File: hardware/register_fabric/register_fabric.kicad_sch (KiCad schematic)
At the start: 417 parts, among them J2 Conn_02x40_Odd_Even, J3 Conn_02x16_Odd_Even, J4 Conn_02x16_Odd_Even, J5 Conn_02x16_Odd_Even, J6 Conn_02x16_Odd_Even, J7 Conn_02x16_Odd_Even, J8 Conn_02x16_Odd_Even, J9 Conn_02x16_Odd_Even, Q109 IRLML6244, Q110 IRLML6402, Q111 IRLML6244, Q112 IRLML6402, Q113 IRLML6244, Q114 IRLML6402, Q115 IRLML6244, Q116 IRLML6402, Q117 IRLML6244, Q118 IRLML6402, Q119 IRLML6244, Q120 IRLML6402, Q121 IRLML6244, Q122 IRLML6402, Q123 IRLML6244, Q124 IRLML6402, Q125 IRLML6244, Q126 IRLML6402, Q127 IRLML6244, Q128 IRLML6402, Q129 IRLML6244, Q130 IRLML6402, Q131 IRLML6244, Q132 IRLML6402, Q133 IRLML6244, Q134 IRLML6402, Q135 IRLML6244, Q136 IRLML6402, Q137 IRLML6244, Q138 IRLML6402, Q139 IRLML6244, Q140 IRLML6402, Q141 IRLML6244, Q142 IRLML6402, Q143 IRLML6244, Q144 IRLML6402, Q145 IRLML6244, Q146 IRLML6402, Q147 IRLML6244, Q148 IRLML6402, Q149 IRLML6244, Q150 IRLML6402, Q151 IRLML6244, Q152 IRLML6402, Q153 IRLML6244, Q154 IRLML6402, Q155 IRLML6244, Q156 IRLML6402, Q157 IRLML6244, Q158 IRLML6402, Q159 IRLML6244, Q160 IRLML6402, Q161 IRLML6244, Q162 IRLML6402, Q163 IRLML6244, Q164 IRLML6402, Q165 IRLML6244, Q166 IRLML6402, Q167 IRLML6244, Q168 IRLML6402, Q169 IRLML6244, Q170 IRLML6402, Q171 IRLML6244, Q172 IRLML6402, Q173 IRLML6244, Q174 IRLML6402, Q175 IRLML6244, Q176 IRLML6402, Q177 IRLML6244, Q178 IRLML6402, Q179 IRLML6244, Q180 IRLML6402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

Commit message: fixed ALU order of Op bits, finished register fabric schematic
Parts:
- removed R244, R245, R246, R247, R248, R249, R250, R251, R252, R253, R254, R255, R256, R257, R258, R259: 1000, Resistor_SMD:R_0402_1005Metric, symbol Device:R
- added R1, R10, R11, R12, R13, R14, R15, R16, R2, R3, R4, R5, R6, R7, R8, R9: 10K, Resistor_SMD:R_0402_1005Metric, symbol Device:R
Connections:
- net +5V: now also R1.1, R10.1, R11.1, R12.1, R13.1, R14.1, R15.1, R16.1, R2.1, R3.1, R4.1, R5.1, R6.1, R7.1, R8.1, R9.1
- net RWEN: now also J2.76 (Pin_76); no longer J2.74 (Pin_74)
- net RSI10: now reaches D194.2 (A), Q216.3 (D), U18.1 (A0)
- net IRWEN: now reaches U19.1, U21.1, U22.1, U23.1, U24.1, U25.1, U26.1
- net IRWEN: now also D198.2 (A), Q224.3 (D)
- net FII2: now reaches D170.2 (A), Q168.3 (D), U89.10 (I1c)
- net at U17.19 (CE), U18.7 (~{Y7}): now also R16.2
- net DII2: now reaches D146.2 (A), J3.15 (Pin_15), J4.15 (Pin_15), J5.15 (Pin_15), J6.15 (Pin_15), J8.15 (Pin_15), J9.15 (Pin_15), Q120.3 (D), U89.11 (I0c)
- net DII1: now reaches D147.2 (A), J3.14 (Pin_14), J4.14 (Pin_14), J5.14 (Pin_14), J6.14 (Pin_14), J8.14 (Pin_14), J9.14 (Pin_14), Q122.3 (D), U89.5 (I0b)
- net WSI0: now reaches D197.2 (A), Q222.3 (D), U20.1 (A0)
- net IFWEN: now reaches D199.2 (A), Q226.3 (D), U24.10, U24.9, U89.1 (S), U90.1 (S)
- net FII3: now reaches D169.2 (A), Q166.3 (D), U89.13 (I1d)
- net DII3: now reaches D145.2 (A), J3.16 (Pin_16), J4.16 (Pin_16), J5.16 (Pin_16), J6.16 (Pin_16), J8.16 (Pin_16), J9.16 (Pin_16), Q118.3 (D), U89.14 (I0d)
- net DII0: now reaches D148.2 (A), J3.13 (Pin_13), J4.13 (Pin_13), J5.13 (Pin_13), J6.13 (Pin_13), J8.13 (Pin_13), J9.13 (Pin_13), Q124.3 (D), U89.2 (I0a)
- net FII0: now reaches D172.2 (A), Q172.3 (D), U89.3 (I1a)
- net FII1: now reaches D171.2 (A), Q170.3 (D), U89.6 (I1b)
- net RAI8: now reaches Q187.1 (G)
- net RAI8: now also J9.3 (Pin_3), U16.2 (A0), U17.2 (A0)
- net RI07: now reaches Q125.1 (G), U1.11 (B7), U10.11 (B7), U12.11 (B7), U14.11 (B7), U16.11 (B7), U4.11 (B7), U6.11 (B7), U8.11 (B7)
- net RI06: now reaches Q127.1 (G), U1.12 (B6), U10.12 (B6), U12.12 (B6), U14.12 (B6), U16.12 (B6), U4.12 (B6), U6.12 (B6), U8.12 (B6)
- net RI05: now reaches Q129.1 (G), U1.13 (B5), U10.13 (B5), U12.13 (B5), U14.13 (B5), U16.13 (B5), U4.13 (B5), U6.13 (B5), U8.13 (B5)
- net RI04: now reaches Q131.1 (G), U1.14 (B4), U10.14 (B4), U12.14 (B4), U14.14 (B4), U16.14 (B4), U4.14 (B4), U6.14 (B4), U8.14 (B4)
- net RI03: now reaches Q133.1 (G), U1.15 (B3), U10.15 (B3), U12.15 (B3), U14.15 (B3), U16.15 (B3), U4.15 (B3), U6.15 (B3), U8.15 (B3)
- net RI02: now reaches Q135.1 (G), U1.16 (B2), U10.16 (B2), U12.16 (B2), U14.16 (B2), U16.16 (B2), U4.16 (B2), U6.16 (B2), U8.16 (B2)
- net RI01: now reaches Q137.1 (G), U1.17 (B1), U10.17 (B1), U12.17 (B1), U14.17 (B1), U16.17 (B1), U4.17 (B1), U6.17 (B1), U8.17 (B1)
- net RI00: now reaches Q139.1 (G), U1.18 (B0), U10.18 (B0), U12.18 (B0), U14.18 (B0), U16.18 (B0), U4.18 (B0), U6.18 (B0), U8.18 (B0)
- net at U14.19 (CE), U2.9 (~{Y6}): now also R13.2
- net RAI0: now reaches J8.3 (Pin_3), U14.2 (A0), U15.2 (A0)
- net RAI0: now also Q203.1 (G)
- net RAI1: now reaches J8.4 (Pin_4), U14.3 (A1), U15.3 (A1)
- net RAI1: now also Q201.1 (G)
- net RAI2: now reaches J8.5 (Pin_5), U14.4 (A2), U15.4 (A2)
- net RAI2: now also Q199.1 (G)
- net RAI3: now reaches J8.6 (Pin_6), U14.5 (A3), U15.5 (A3)
- net RAI3: now also Q197.1 (G)
- net RAI4: now reaches J8.7 (Pin_7), U14.6 (A4), U15.6 (A4)
- net RAI4: now also Q195.1 (G)
- net RAI5: now reaches J8.8 (Pin_8), U14.7 (A5), U15.7 (A5)
- net RAI5: now also Q193.1 (G)
- net RAI6: now reaches J8.9 (Pin_9), U14.8 (A6), U15.8 (A6)
- net RAI6: now also Q191.1 (G)
- net RAI7: now reaches J8.10 (Pin_10), U14.9 (A7), U15.9 (A7)
- net RAI7: now also Q189.1 (G)
- net FII5: now reaches D167.2 (A), Q162.3 (D), U90.6 (I1b)
- net at U12.19 (CE), U2.10 (~{Y5}): now also R11.2
- net COUT: now reaches J7.5 (Pin_5), U12.4 (A2), U13.4 (A2)
- net COUT: now also J2.74 (Pin_74)
- net WSI1: now reaches D196.2 (A), Q220.3 (D), U20.2 (A1)
- net RSI02: now reaches D189.2 (A), Q206.3 (D), U2.3 (A2)
- net RI12: now reaches Q151.1 (G), U11.16 (B2), U13.16 (B2), U15.16 (B2), U17.16 (B2), U3.16 (B2), U5.16 (B2), U7.16 (B2), U9.16 (B2)
- net RSI11: now reaches D193.2 (A), Q214.3 (D), U18.2 (A1)
- net RI17: now reaches Q141.1 (G), U11.11 (B7), U13.11 (B7), U15.11 (B7), U17.11 (B7), U3.11 (B7), U5.11 (B7), U7.11 (B7), U9.11 (B7)
- net RI16: now reaches Q143.1 (G), U11.12 (B6), U13.12 (B6), U15.12 (B6), U17.12 (B6), U3.12 (B6), U5.12 (B6), U7.12 (B6), U9.12 (B6)
- net RI15: now reaches Q145.1 (G), U11.13 (B5), U13.13 (B5), U15.13 (B5), U17.13 (B5), U3.13 (B5), U5.13 (B5), U7.13 (B5), U9.13 (B5)
- net RI14: now reaches Q147.1 (G), U11.14 (B4), U13.14 (B4), U15.14 (B4), U17.14 (B4), U3.14 (B4), U5.14 (B4), U7.14 (B4), U9.14 (B4)
- net RI13: now reaches Q149.1 (G), U11.15 (B3), U13.15 (B3), U15.15 (B3), U17.15 (B3), U3.15 (B3), U5.15 (B3), U7.15 (B3), U9.15 (B3)
- net RI11: now reaches Q153.1 (G), U11.17 (B1), U13.17 (B1), U15.17 (B1), U17.17 (B1), U3.17 (B1), U5.17 (B1), U7.17 (B1), U9.17 (B1)
- net RI10: now reaches Q155.1 (G), U11.18 (B0), U13.18 (B0), U15.18 (B0), U17.18 (B0), U3.18 (B0), U5.18 (B0), U7.18 (B0), U9.18 (B0)
- net at U15.19 (CE), U18.9 (~{Y6}): now also R14.2
- net FII6: now reaches D166.2 (A), Q160.3 (D), U90.10 (I1c)
- net FII7: now reaches D165.2 (A), Q158.3 (D), U90.13 (I1d)
- net at J2.2 (Pin_2), J2.20 (Pin_20), J2.38 (Pin_38)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: no longer J2.76 (Pin_76)
- net RSI00: now reaches D191.2 (A), Q210.3 (D), U2.1 (A0)
- net DII4: now reaches D144.2 (A), J3.17 (Pin_17), J4.17 (Pin_17), J5.17 (Pin_17), J6.17 (Pin_17), J8.17 (Pin_17), J9.17 (Pin_17), Q116.3 (D), U90.2 (I0a)
- net DII5: now reaches D143.2 (A), J3.18 (Pin_18), J4.18 (Pin_18), J5.18 (Pin_18), J6.18 (Pin_18), J8.18 (Pin_18), J9.18 (Pin_18), Q114.3 (D), U90.5 (I0b)
- net DII6: now reaches D142.2 (A), J3.19 (Pin_19), J4.19 (Pin_19), J5.19 (Pin_19), J6.19 (Pin_19), J8.19 (Pin_19), J9.19 (Pin_19), Q112.3 (D), U90.11 (I0c)
- net DII7: now reaches D141.2 (A), J3.20 (Pin_20), J4.20 (Pin_20), J5.20 (Pin_20), J6.20 (Pin_20), J8.20 (Pin_20), J9.20 (Pin_20), Q110.3 (D), U90.14 (I0d)
- net ICLK: now reaches D200.2 (A), J3.25 (Pin_25), J4.25 (Pin_25), J5.25 (Pin_25), J6.25 (Pin_25), J7.25 (Pin_25), J8.25 (Pin_25), J9.25 (Pin_25), Q228.3 (D)
- net I!CLR: now reaches D201.2 (A), J3.29 (Pin_29), J4.29 (Pin_29), J5.29 (Pin_29), J6.29 (Pin_29), J7.29 (Pin_29), J8.29 (Pin_29), J9.29 (Pin_29), Q230.3 (D)
- net at U16.19 (CE), U2.7 (~{Y7}): now also R15.2
- net at U2.14 (~{Y1}), U4.19 (CE): now also R3.2
- net RAI11: now reaches Q181.1 (G)
- net RAI11: now also J9.6 (Pin_6), U16.5 (A3), U17.5 (A3)
- net RSI12: now reaches D192.2 (A), Q212.3 (D), U18.3 (A2)
- net RAI9: now reaches Q185.1 (G)
- net RAI9: now also J9.4 (Pin_4), U16.3 (A1), U17.3 (A1)
- net at U10.19 (CE), U2.11 (~{Y4}): now also R9.2
- net WSI2: now reaches D195.2 (A), Q218.3 (D), U20.3 (A2)
- net at U18.14 (~{Y1}), U5.19 (CE): now also R4.2
- net RAI15: now reaches J9.10 (Pin_10), U16.9 (A7), U17.9 (A7)
- net RAI15: now also Q173.1 (G)
- net RAI10: now reaches J9.5 (Pin_5), U16.4 (A2), U17.4 (A2)
- net RAI10: now also Q183.1 (G)
- net RAI12: now reaches J9.7 (Pin_7), U16.6 (A4), U17.6 (A4)
- net RAI12: now also Q179.1 (G)
- net RAI13: now reaches J9.8 (Pin_8), U16.7 (A5), U17.7 (A5)
- net RAI13: now also Q177.1 (G)
- net RAI14: now reaches J9.9 (Pin_9), U16.8 (A6), U17.8 (A6)
- net RAI14: now also Q175.1 (G)
- net at U11.19 (CE), U18.11 (~{Y4}): now also R10.2
- net at U18.13 (~{Y2}), U7.19 (CE): now also R6.2
- net at U2.13 (~{Y2}), U6.19 (CE): now also R5.2
- net at U13.19 (CE), U18.10 (~{Y5}): now also R12.2
- net RSI01: now reaches D190.2 (A), Q208.3 (D), U2.2 (A1)
- net at U18.12 (~{Y3}), U9.19 (CE): now also R8.2
- net at U2.12 (~{Y3}), U8.19 (CE): now also R7.2
- net at U18.15 (~{Y0}), U3.19 (CE): now also R2.2
- net at U1.19 (CE), U2.15 (~{Y0}): now also R1.2
- net FII4: now reaches D168.2 (A), Q164.3 (D), U90.3 (I1a)
- no-connect marks 13 -> 15
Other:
- moved on the sheet: C2, C25, C3

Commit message: started work on register fabric PCB layout, grouped LEDs
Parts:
- U1, U10, U11, U12, U13, U14, U15, U16, U17, U3, U4, U5, U6, U7, U8, U9: footprint Package_SO:SO-20_12.8x7.5mm_P1.27mm -> Package_SO:TSSOP-20_4.4x6.5mm_P0.65mm
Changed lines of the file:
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@@
 			)
 		)
-		(property "Footprint" "Package_SO:SO-20_12.8x7.5mm_P1.27mm"
+		(property "Footprint" "Package_SO:TSSOP-20_4.4x6.5mm_P0.65mm"
 			(at 1671.32 1037.59 0)
 			(effects
@@
 			)
 		)
-		(property "Footprint" "Package_SO:SO-20_12.8x7.5mm_P1.27mm"
+		(property "Footprint" "Package_SO:TSSOP-20_4.4x6.5mm_P0.65mm"
 			(at 1671.32 920.75 0)
 			(effects
@@
 			)
 		)
-		(property "Footprint" "Package_SO:SO-20_12.8x7.5mm_P1.27mm"
+		(property "Footprint" "Package_SO:TSSOP-20_4.4x6.5mm_P0.65mm"
 			(at 1671.32 1096.01 0)
 			(effects
@@
 			)
 		)
-		(property "Footprint" "Package_SO:SO-20_12.8x7.5mm_P1.27mm"
+		(property "Footprint" "Package_SO:TSSOP-20_4.4x6.5mm_P0.65mm"
 			(at 1671.32 862.33 0)
 			(effects
@@
 			)
 		)
-		(property "Footprint" "Package_SO:SO-20_12.8x7.5mm_P1.27mm"
+		(property "Footprint" "Package_SO:TSSOP-20_4.4x6.5mm_P0.65mm"
 			(at 1671.32 570.23 0)
 			(effects
@@
 			)
 		)
-		(property "Footprint" "Package_SO:SO-20_12.8x7.5mm_P1.27mm"
+		(property "Footprint" "Package_SO:TSSOP-20_4.4x6.5mm_P0.65mm"
 			(at 1671.32 979.17 0)
 			(effects
@@
 			)
 		)
-		(property "Footprint" "Package_SO:SO-20_12.8x7.5mm_P1.27mm"
+		(property "Footprint" "Package_SO:TSSOP-20_4.4x6.5mm_P0.65mm"
 			(at 1671.32 803.91 0)
 			(effects
@@
 			)
 		)
-		(property "Footprint" "Package_SO:SO-20_12.8x7.5mm_P1.27mm"
+		(property "Footprint" "Package_SO:TSSOP-20_4.4x6.5mm_P0.65mm"
 			(at 1671.32 745.49 0)
 			(effects
@@
 			)
 		)
-		(property "Footprint" "Package_SO:SO-20_12.8x7.5mm_P1.27mm"
+		(property "Footprint" "Package_SO:TSSOP-20_4.4x6.5mm_P0.65mm"
 			(at 1671.32 394.97 0)
 			(effects
@@
 			)
 		)
-		(property "Footprint" "Package_SO:SO-20_12.8x7.5mm_P1.27mm"
+		(property "Footprint" "Package_SO:TSSOP-20_4.4x6.5mm_P0.65mm"
 			(at 1671.32 1154.43 0)
 			(effects
@@
 			)
 		)
-		(property "Footprint" "Package_SO:SO-20_12.8x7.5mm_P1.27mm"
+		(property "Footprint" "Package_SO:TSSOP-20_4.4x6.5mm_P0.65mm"
 			(at 1671.32 1212.85 0)
 			(effects
@@
 			)
 		)
-		(property "Footprint" "Package_SO:SO-20_12.8x7.5mm_P1.27mm"
+		(property "Footprint" "Package_SO:TSSOP-20_4.4x6.5mm_P0.65mm"
 			(at 1671.32 687.07 0)
 			(effects
@@
 		(on_board yes)
 		(dnp no)
-		(fields_autoplaced yes)
 		(property "Reference" "U4"
 			(at 1673.4633 433.07 0)
@@
 			)
 		)
-		(property "Footprint" "Package_SO:SO-20_12.8x7.5mm_P1.27mm"
+		(property "Footprint" "Package_SO:TSSOP-20_4.4x6.5mm_P0.65mm"
 			(at 1671.32 453.39 0)
 			(effects
@@
 			)
 		)
-		(property "Footprint" "Package_SO:SO-20_12.8x7.5mm_P1.27mm"
+		(property "Footprint" "Package_SO:TSSOP-20_4.4x6.5mm_P0.65mm"
 			(at 1671.32 628.65 0)
 			(effects
@@
 			)
 		)
-		(property "Footprint" "Package_SO:SO-20_12.8x7.5mm_P1.27mm"
+		(property "Footprint" "Package_SO:TSSOP-20_4.4x6.5mm_P0.65mm"
 			(at 1671.32 511.81 0)
 			(effects
@@
 			)
 		)
-		(property "Footprint" "Package_SO:SO-20_12.8x7.5mm_P1.27mm"
+		(property "Footprint" "Package_SO:TSSOP-20_4.4x6.5mm_P0.65mm"
 			(at 1671.32 336.55 0)
 			(effects

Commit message: finished Rev A of register fabric pcb
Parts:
- added C33, C34, C35, C36: 330nF, Capacitor_SMD:C_0402_1005Metric, symbol Device:C
- added D202: LED, LED_SMD:LED_0402_1005Metric, symbol Device:LED
- added R244: 1000, Resistor_SMD:R_0402_1005Metric, symbol Device:R
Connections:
- net +5V: now also C33.1, C34.1, C35.1, C36.1, D202.2 (A)
- net GND: now also J2.1 (Pin_1), J2.19 (Pin_19), J2.2 (Pin_2), J2.20 (Pin_20), J2.37 (Pin_37), J2.38 (Pin_38), J2.55 (Pin_55), J2.56 (Pin_56), J2.63 (Pin_63), J2.64 (Pin_64), J2.69 (Pin_69), J2.72 (Pin_72), J2.79 (Pin_79), J2.80 (Pin_80), C33.2, C34.2, C35.2, C36.2, R244.1
- new net: D202.1 (K), R244.2

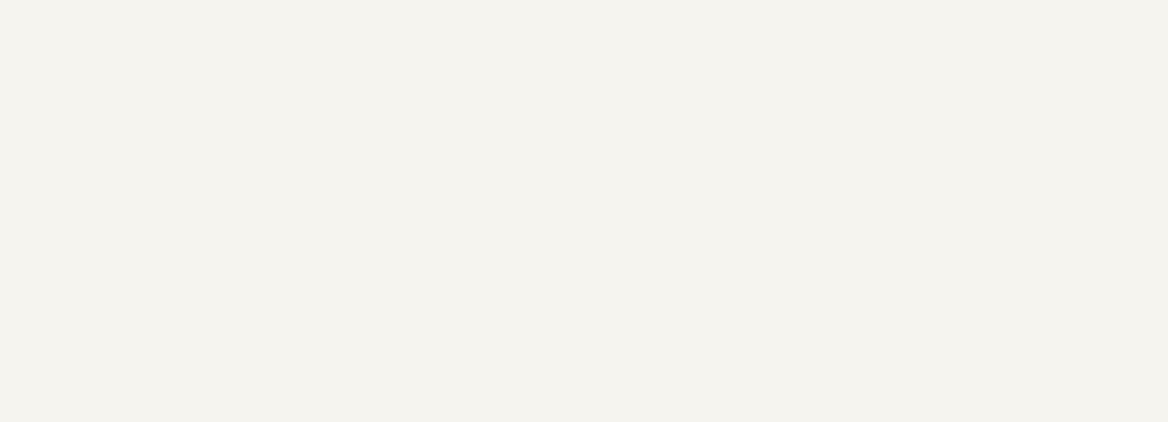
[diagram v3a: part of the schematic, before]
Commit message: added fiducials and markers to ALU, started on register fabric
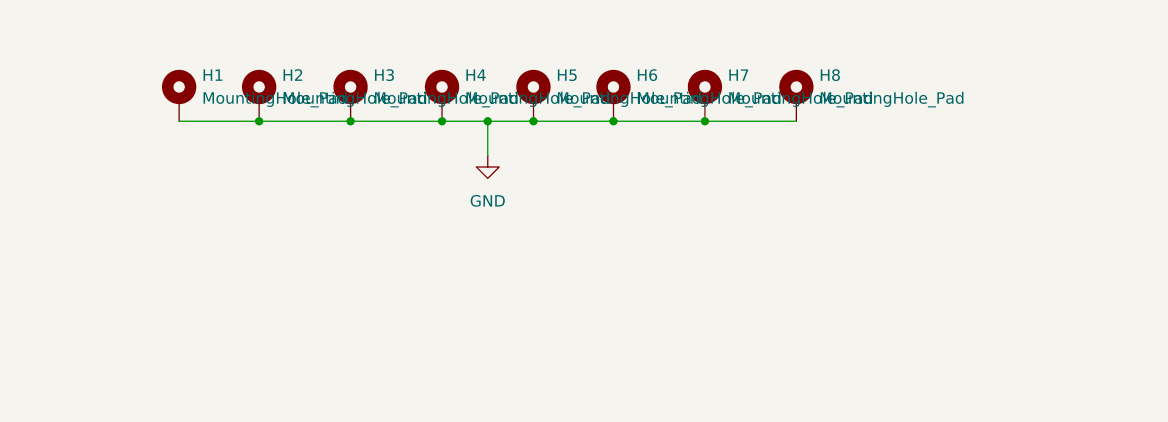
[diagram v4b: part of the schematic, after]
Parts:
- added H1, H2, H3, H4, H5, H6, H7, H8: MountingHole_Pad, MountingHole:MountingHole_3.2mm_M3_ISO7380_Pad_TopBottom, symbol Mechanical:MountingHole_Pad
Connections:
- net GND: now also H1.1, H2.1, H3.1, H4.1, H5.1, H6.1, H7.1, H8.1

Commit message: small fixes on register fabric
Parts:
- R1, R10, R11, R12, R13, R14, R15, R16, R2, R21, R22, R23, R24, R25, R26, R27, R28, R29, R3, R30, R31, R32, R33, R34, R35, R36, R37, R38, R39, R4, R40, R41, R45, R46, R47, R48, R49, R5, R50, R51, R52, R6, R7, R8, R9: value 10K -> 100K
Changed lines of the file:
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@@
 			)
 		)
-		(property "Value" "10K"
+		(property "Value" "100K"
 			(at 1630.68 1046.48 90)
 			(effects
@@
 			)
 		)
-		(property "Value" "10K"
+		(property "Value" "100K"
 			(at 424.18 807.7199 0)
 			(effects
@@
 			)
 		)
-		(property "Value" "10K"
+		(property "Value" "100K"
 			(at 553.72 807.7199 0)
 			(effects
@@
 			)
 		)
-		(property "Value" "10K"
+		(property "Value" "100K"
 			(at 643.89 384.8099 0)
 			(effects
@@
 			)
 		)
-		(property "Value" "10K"
+		(property "Value" "100K"
 			(at 904.24 384.8099 0)
 			(effects
@@
 			)
 		)
-		(property "Value" "10K"
+		(property "Value" "100K"
 			(at 1621.79 520.7 90)
 			(effects
@@
 			)
 		)
-		(property "Value" "10K"
+		(property "Value" "100K"
 			(at 294.64 386.0799 0)
 			(effects
@@
 			)
 		)
-		(property "Value" "10K"
+		(property "Value" "100K"
 			(at 337.82 386.0799 0)
 			(effects
@@
 			)
 		)
-		(property "Value" "10K"
+		(property "Value" "100K"
 			(at 596.9 933.4499 0)
 			(effects
@@
 			)
 		)
-		(property "Value" "10K"
+		(property "Value" "100K"
 			(at 1630.68 1104.9 90)
 			(effects
@@
 			)
 		)
-		(property "Value" "10K"
+		(property "Value" "100K"
 			(at 1621.79 988.06 90)
 			(effects
@@
 			)
 		)
-		(property "Value" "10K"
+		(property "Value" "100K"
 			(at 1621.79 754.38 90)
 			(effects
@@
 			)
 		)
-		(property "Value" "10K"
+		(property "Value" "100K"
 			(at 817.88 384.8099 0)
 			(effects
@@
 			)
 		)
-		(property "Value" "10K"
+		(property "Value" "100K"
 			(at 1621.79 579.12 90)
 			(effects
@@
 			)
 		)
-		(property "Value" "10K"
+		(property "Value" "100K"
 			(at 510.54 807.7199 0)
 			(effects
@@
 			)
 		)
-		(property "Value" "10K"
+		(property "Value" "100K"
 			(at 553.72 933.4499 0)
 			(effects
@@
 			)
 		)
-		(property "Value" "10K"
+		(property "Value" "100K"
 			(at 1630.68 1163.32 90)
 			(effects
@@
 			)
 		)
-		(property "Value" "10K"
+		(property "Value" "100K"
 			(at 337.82 807.7199 0)
 			(effects
@@
 			)
 		)
-		(property "Value" "10K"
+		(property "Value" "100K"
 			(at 1621.79 403.86 90)
 			(effects
@@
 			)
 		)
-		(property "Value" "10K"
+		(property "Value" "100K"
 			(at 1621.79 871.22 90)
 			(effects
@@
 			)
 		)
-		(property "Value" "10K"
+		(property "Value" "100K"
 			(at 424.18 933.4499 0)
 			(effects
@@
 			)
 		)
-		(property "Value" "10K"
+		(property "Value" "100K"
 			(at 687.07 384.8099 0)
 			(effects
@@
 			)
 		)
-		(property "Value" "10K"
+		(property "Value" "100K"
 			(at 467.36 386.0799 0)
 			(effects
@@
 			)
 		)
-		(property "Value" "10K"
+		(property "Value" "100K"
 			(at 1621.79 637.54 90)
 			(effects
@@
 			)
 		)
-		(property "Value" "10K"
+		(property "Value" "100K"
 			(at 730.25 384.8099 0)
 			(effects
@@
 			)
 		)
-		(property "Value" "10K"
+		(property "Value" "100K"
 			(at 947.42 384.8099 0)
 			(effects
@@
 			)
 		)
-		(property "Value" "10K"
+		(property "Value" "100K"
 			(at 596.9 807.7199 0)
 			(effects
@@
 			)
 		)
-		(property "Value" "10K"
+		(property "Value" "100K"
 			(at 294.64 933.4499 0)
 			(effects
@@
 			)
 		)
-		(property "Value" "10K"
+		(property "Value" "100K"
 			(at 337.82 933.4499 0)
 			(effects
@@
 			)
 		)
-		(property "Value" "10K"
+		(property "Value" "100K"
 			(at 510.54 386.0799 0)
 			(effects
@@
 			)
 		)
-		(property "Value" "10K"
+		(property "Value" "100K"
 			(at 1621.79 345.44 90)
 			(effects
@@
 			)
 		)
-		(property "Value" "10K"
+		(property "Value" "100K"
 			(at 861.06 384.8099 0)
 			(effects
@@
 			)
 		)
-		(property "Value" "10K"
+		(property "Value" "100K"
 			(at 1621.79 929.64 90)
 			(effects
@@
 			)
 		)
-		(property "Value" "10K"
+		(property "Value" "100K"
 			(at 381 386.0799 0)
 			(effects
@@
 			)
 		)
-		(property "Value" "10K"
+		(property "Value" "100K"
 			(at 294.64 807.7199 0)
 			(effects
@@
 			)
 		)
-		(property "Value" "10K"
+		(property "Value" "100K"
 			(at 1621.79 462.28 90)
 			(effects
@@
 			)
 		)
-		(property "Value" "10K"
+		(property "Value" "100K"
 			(at 381 807.7199 0)
 			(effects
@@
 			)
 		)
-		(property "Value" "10K"
+		(property "Value" "100K"
 			(at 553.72 386.0799 0)
 			(effects
@@
 			)
 		)
-		(property "Value" "10K"
+		(property "Value" "100K"
 			(at 381 933.4499 0)
 			(effects
@@
 			)
 		)
-		(property "Value" "10K"
+		(property "Value" "100K"
 			(at 1630.68 1221.74 90)
 			(effects
@@
 			)
 		)
-		(property "Value" "10K"
+		(property "Value" "100K"
 			(at 510.54 933.4499 0)
 			(effects
@@
 			)
 		)
-		(property "Value" "10K"
+		(property "Value" "100K"
 			(at 1621.79 812.8 90)
 			(effects
@@
 			)
 		)
-		(property "Value" "10K"
+		(property "Value" "100K"
 			(at 467.36 933.4499 0)
 			(effects
@@
 			)
 		)
-		(property "Value" "10K"
+		(property "Value" "100K"
 			(at 1621.79 695.96 90)
 			(effects
@@
 			)
 		)
-		(property "Value" "10K"
+		(property "Value" "100K"
 			(at 467.36 807.7199 0)
 			(effects
